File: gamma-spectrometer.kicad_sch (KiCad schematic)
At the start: 62 parts, among them J1 *, J2 *, J3 *, J4 *, Q1 2N7002, Q2 2N7002, SW1 *, U1 Pico 2, U2 OPA357AIDBVR, U3 TLV3201AIDBVR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

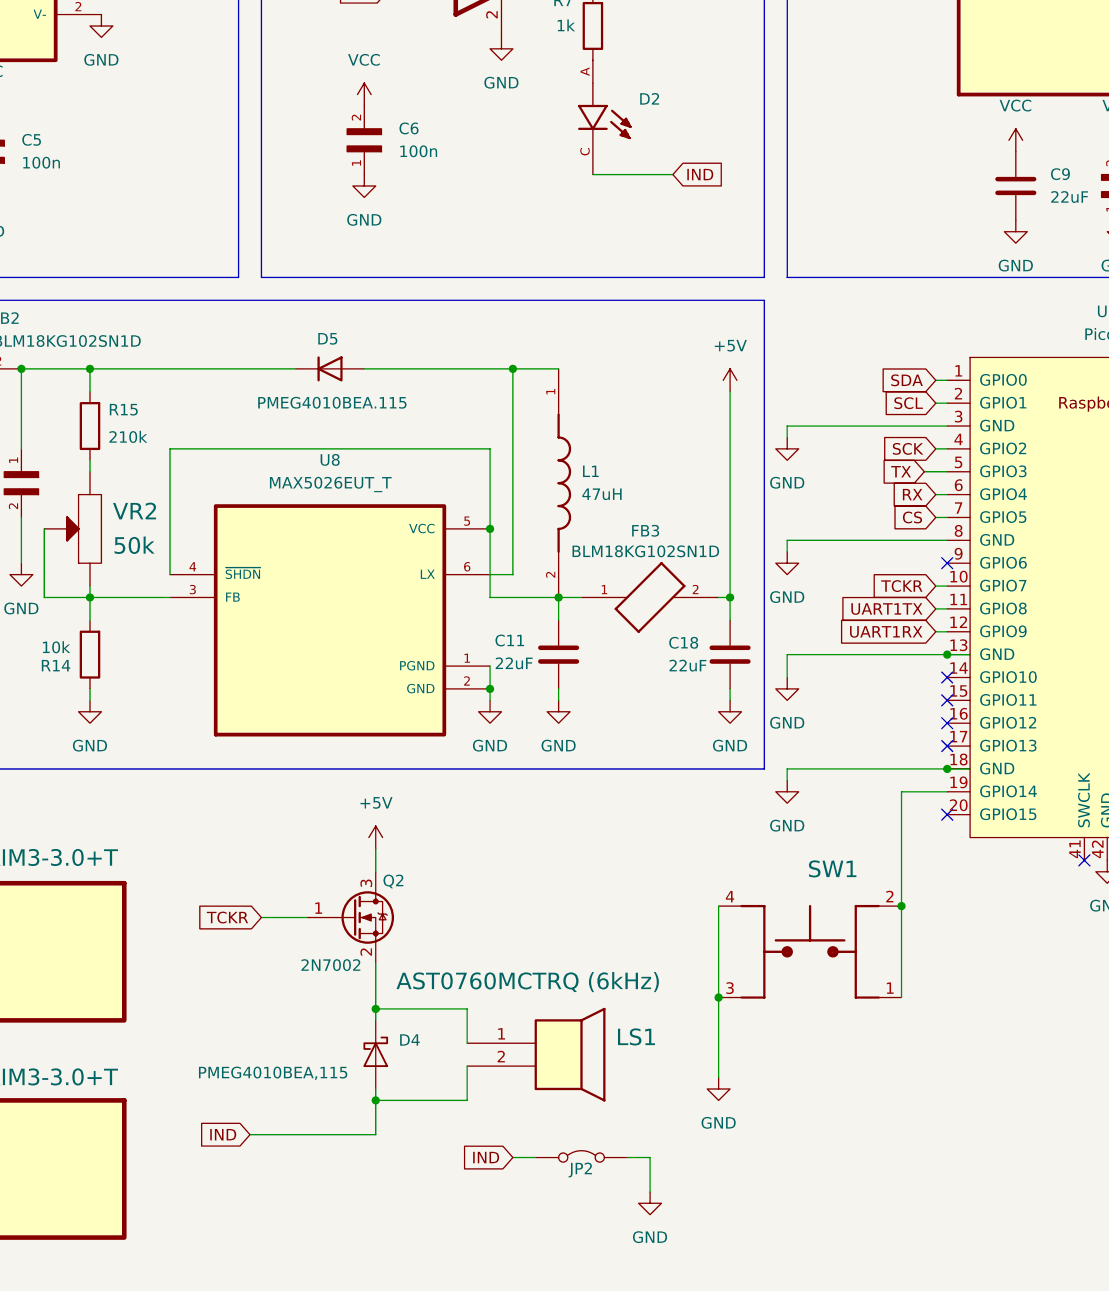
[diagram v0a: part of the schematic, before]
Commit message: Changed schematic for default I2C pins
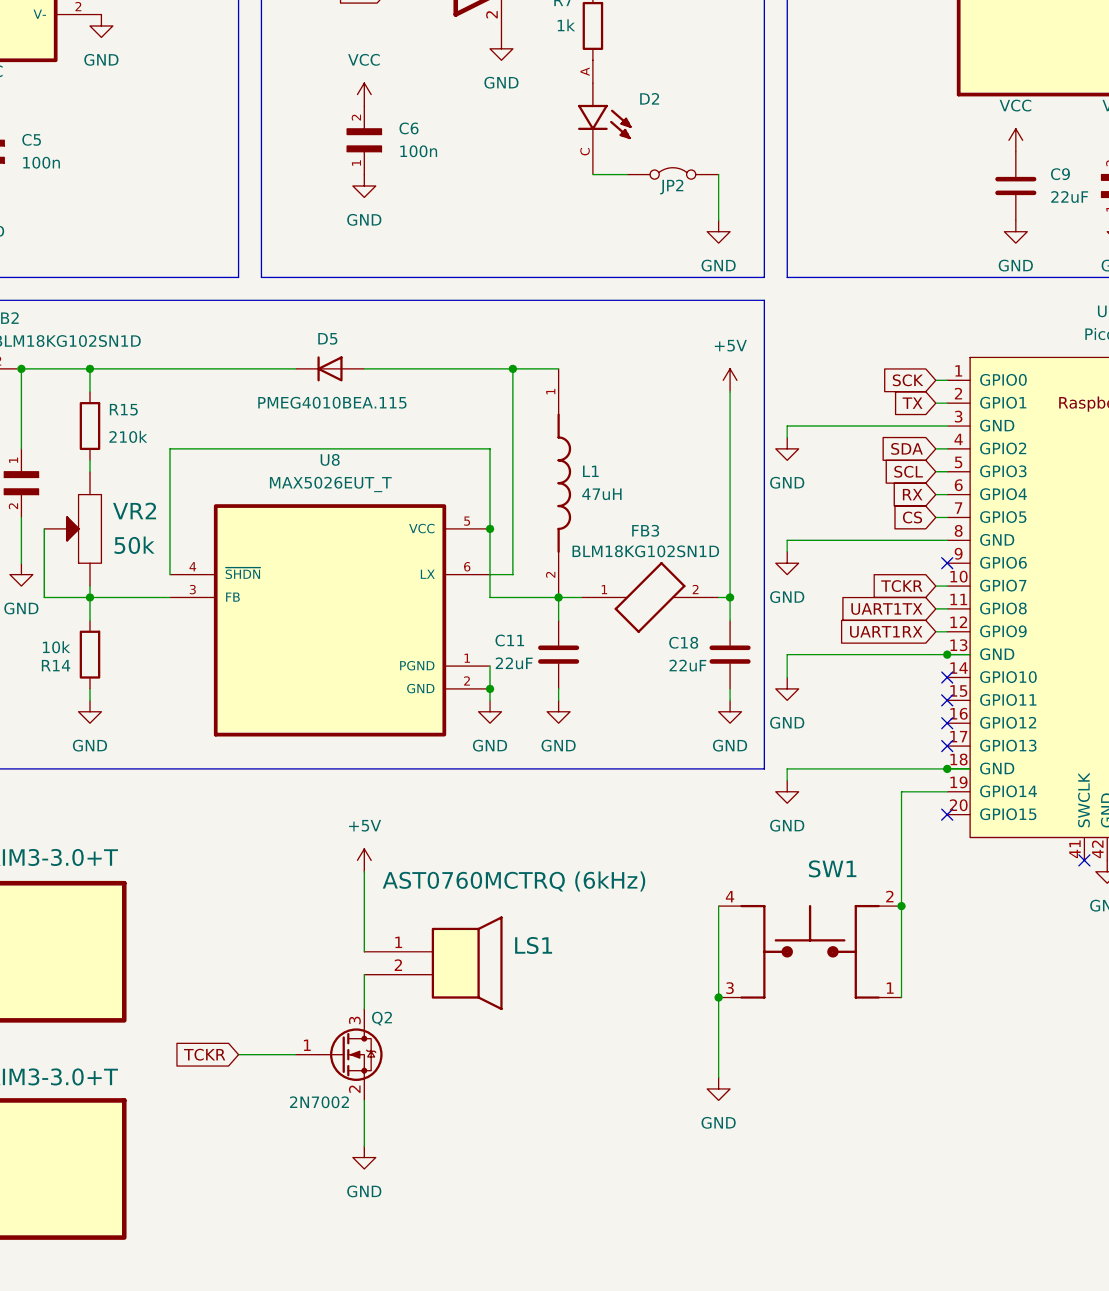
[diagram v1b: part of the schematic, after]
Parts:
- removed D4: PMEG4010BEA,115, Diode_SMD:D_SOD-323F, symbol Diode:PMEG4010EJ
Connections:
- net +5V: now also LS1.1; no longer Q2.3 (D)
- net GND: now also Q2.2 (S)
- net SCK: now also U1.1 (GPIO0); no longer U1.4 (GPIO2)
- net SCL: now also U1.5 (GPIO3); no longer U1.2 (GPIO1)
- net SDA: now also U1.4 (GPIO2); no longer U1.1 (GPIO0)
- net TX: now also U1.2 (GPIO1); no longer U1.5 (GPIO3)
- net IND: no longer names the net of D2.C, JP2.1 (A)
- net IND: no longer LS1.2
- new net: LS1.2, Q2.3 (D)
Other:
- moved on the sheet: JP2, LS1

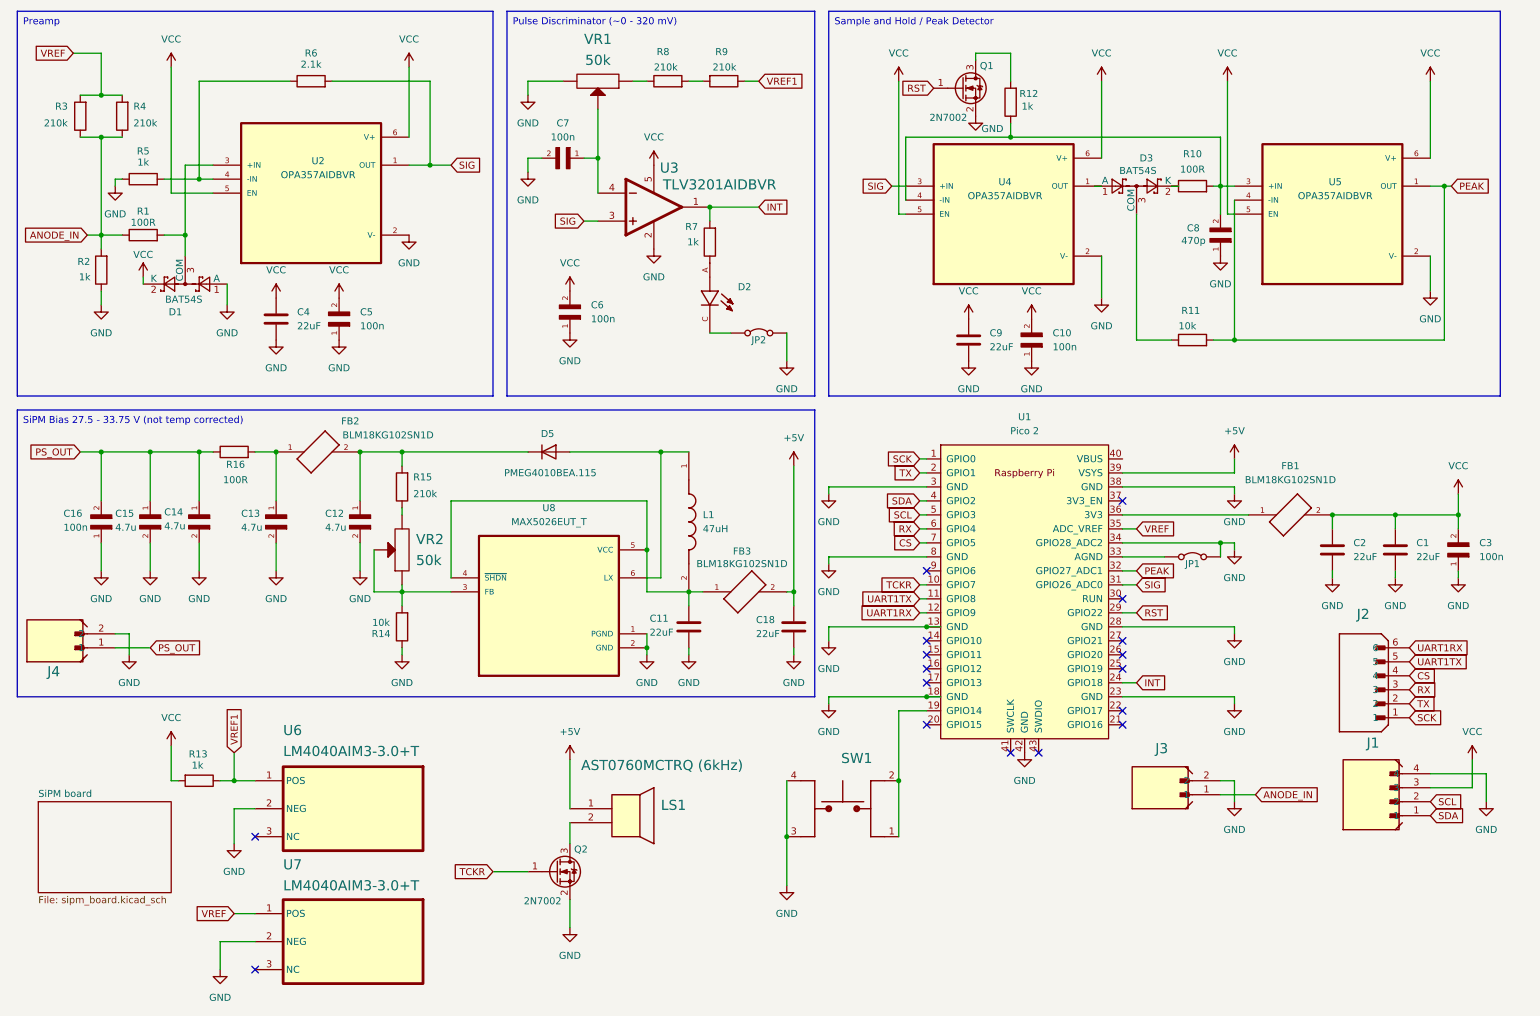
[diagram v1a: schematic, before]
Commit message: Added gain regulator. MHF3 connector for signal line.
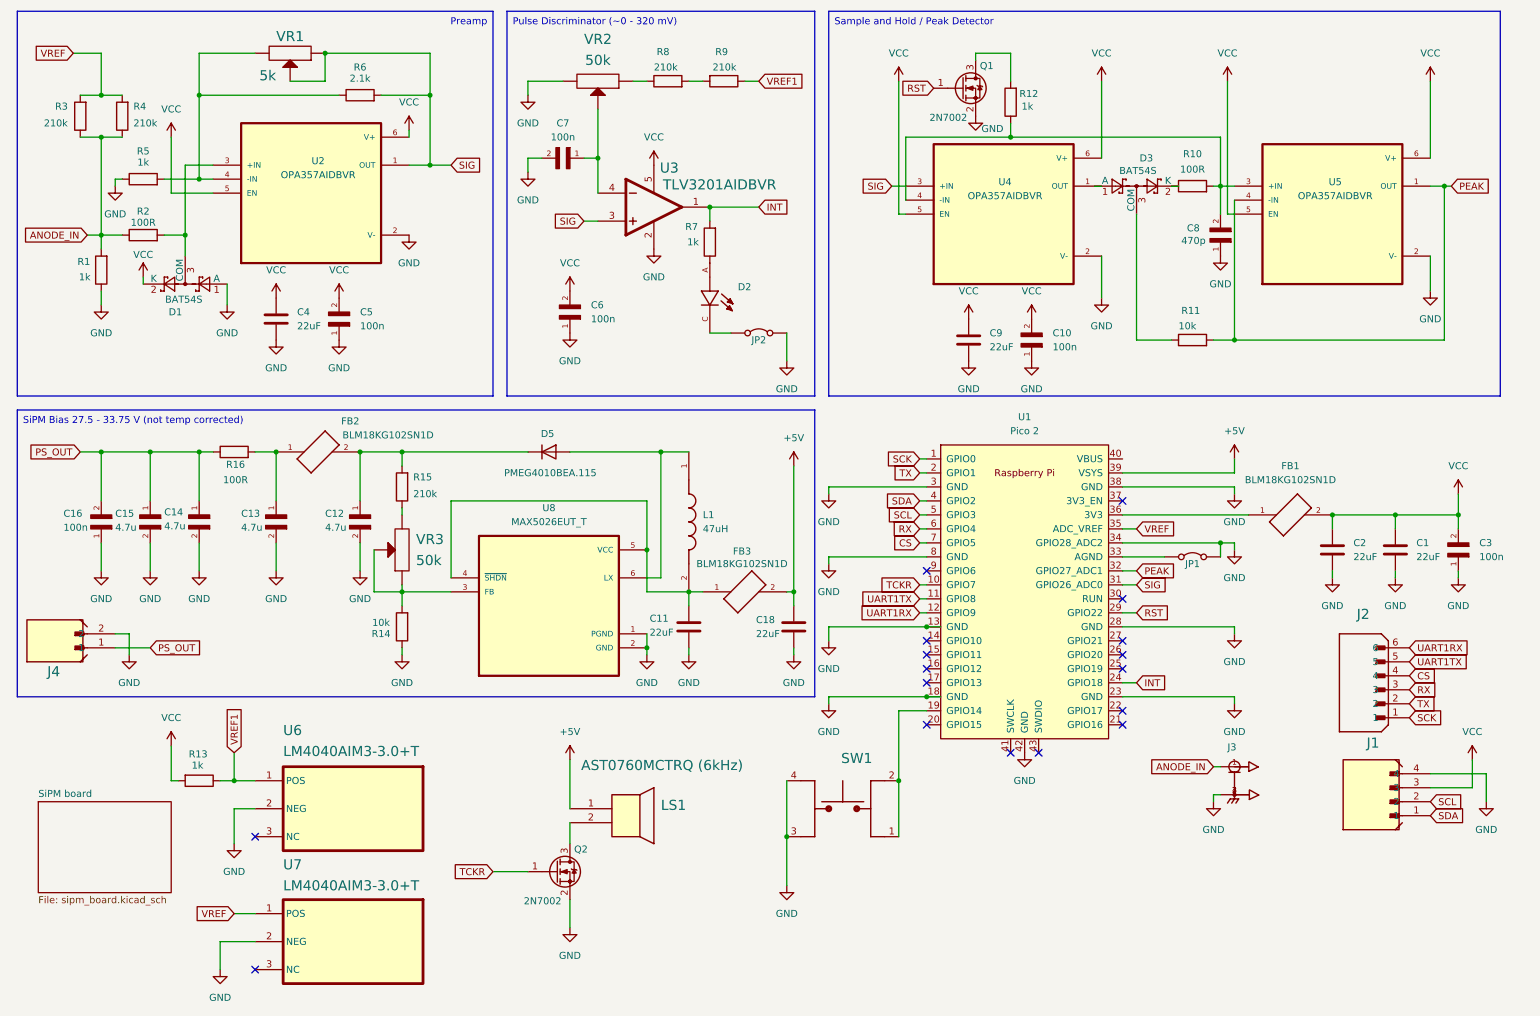
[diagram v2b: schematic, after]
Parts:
- removed J3: *, B2B-PH-K-S_LF__SN_:JST_B2B-PH-K-S(LF)(SN), symbol B2B-PH-K-S_LF__SN_:B2B-PH-K-S(LF)(SN)
- added J3: 20449-001E-03, 20449-001E-03:IPEX_20449-001E-03, symbol 20449-001E-03:20449-001E-03
- added VR1: 5k, 3296W-1-502LF:TRIM_3296W-1-502LF, symbol 3296W-1-502LF-1:3296W-1-502LF_1
- renumbered R2 to R1, R1 to R2, VR1 to VR2, VR2 to VR3
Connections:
- net ANODE_IN: now also J3.1
- net GND: now also J3.2, J3.3, J3.4
- net SIG: now also VR1.1 (CCW), VR1.2 (WIPER)
- net at R5.2, R6.1, U2.4 (-IN): now also VR1.3 (CW)
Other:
- moved on the sheet: R6

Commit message: BDG4-01 module boards design
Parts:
- removed C4: 22uF, CL10A226MP8NUNE:CAPC1608X90N, symbol Device:C
- removed C5: 100n, CL10B104KC8NNNC:CAPC1608X90N, symbol CL10B104KC8NNNC:CL10B104KC8NNNC
- removed D1: BAT54S, Package_TO_SOT_SMD:SOT-23, symbol Diode:BAT54S
- removed J3: 20449-001E-03, 20449-001E-03:IPEX_20449-001E-03, symbol 20449-001E-03:20449-001E-03
- removed J4: *, B2B-PH-K-S_LF__SN_:JST_B2B-PH-K-S(LF)(SN), symbol B2B-PH-K-S_LF__SN_:B2B-PH-K-S(LF)(SN)
- removed LS1: AST0760MCTRQ (6kHz), AST0760MCTRQ:AST0760_MAL, symbol AST0760MCTRQ:AST0760MCTRQ
- removed Q2: 2N7002, Package_TO_SOT_SMD:SOT-23, symbol Transistor_FET:2N7002
- removed R1, R5: 1k, ERJ3EKF2103V:RES_ERJ3EKF2103V, symbol Device:R
- removed R2: 100R, ERJ3EKF2103V:RES_ERJ3EKF2103V, symbol Device:R
- removed R3, R4: 210k, ERJ3EKF2103V:RES_ERJ3EKF2103V, symbol Device:R
- removed R6: 2.1k, ERJ3EKF2103V:RES_ERJ3EKF2103V, symbol Device:R
- removed SW1: *, SW_TL3305AF160QG:SW_TL3305AF160QG, symbol TL3305AF160QG:TL3305AF160QG
- removed U2: OPA357AIDBVR, OPA357AIDBVR:SOT95P280X145-6N, symbol OPA357AIDBVR:OPA357AIDBVR
- removed U7: LM4040AIM3-3.0+T, LM4040AIM3-3_0-T:SOT95P237X112-3N, symbol LM4040AIM3-3_0-T:LM4040AIM3-3_0-T
- removed VR1: 5k, 3296W-1-502LF:TRIM_3296W-1-502LF, symbol 3296W-1-502LF-1:3296W-1-502LF_1
- removed VR2: 50k, 3296W-1-503LF:TRIM_3296W-1-503LF, symbol 3296W-1-503LF:3296W-1-503LF
- added VR1: 50k, 3296W-1-503LF:TRIM_3296W-1-503LF, symbol 3296W-1-503LF:3296W-1-503LF
- R7: value 1k -> 210k
- R8: value 210k -> 1k
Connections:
- net GND: now also C6.2, C7.1, VR1.1 (CCW); no longer C6.1, C7.2
- net INT: now also R8.2; no longer R7.2
- net VCC: now also C7.2; no longer C6.2
- net VREF: now also R13.1, R9.1, U6.1 (POS); no longer U1.35 (ADC_VREF)
- net VREF1: now also U1.35 (ADC_VREF); no longer R13.1, R9.1, U6.1 (POS)
- net at C11.1, FB3.1, L1.2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: now also D5.2 (A), L1.1, U8.6 (LX)
- net at R7.1: now also VR1.3 (CW); no longer D2.A
- net at R9.2: now also R7.2; no longer R8.2
- net at R8.1: now also D2.A
- net at U3.4 (IN-): now also C6.1, VR1.2 (WIPER); no longer C7.1
- net VBUS: now reaches U1.40 (VBUS)
- net TCKR: no longer names the net of U1.10 (GPIO7)
- no-connect marks 17 -> 18
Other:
- added sheet Amplifier (preamp.kicad_sch)
- moved on the sheet: C1, C11, C12, C13, C14, C15, C16, C18, C2, C3, D5, FB1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

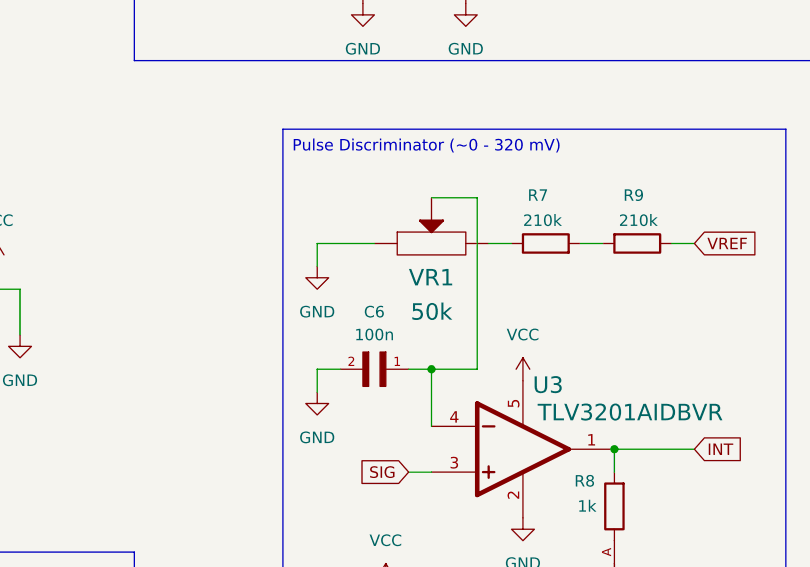
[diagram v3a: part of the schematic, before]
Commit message: PCB changes for more precise assembling
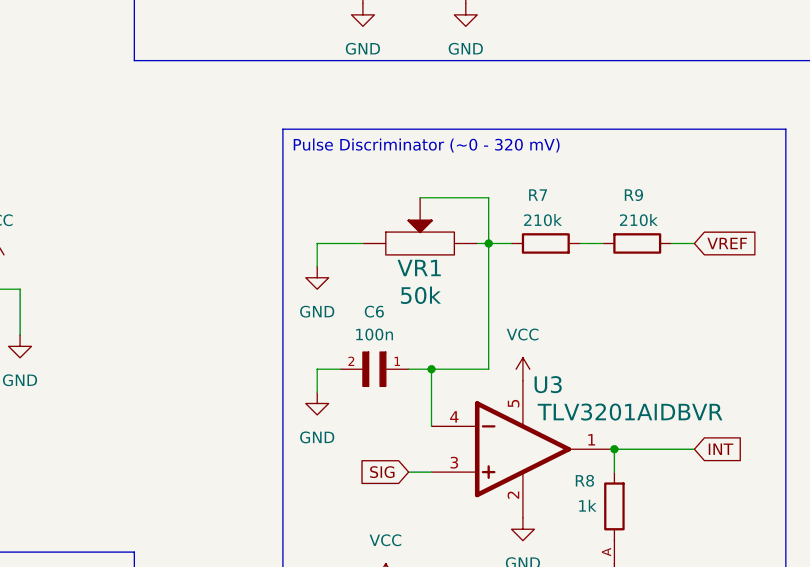
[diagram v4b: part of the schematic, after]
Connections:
- net at C6.1, U3.4 (IN-), VR1.2 (WIPER): now also R7.1, VR1.3 (CW)
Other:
- moved on the sheet: VR1
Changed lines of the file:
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@@
 		(title "Gamma Spectrometer")
 		(date "2025-01-17")
-		(rev "0.1.0")
+		(rev "0.1.1")
 		(company "Vadym Vikulin")
 	)
@@
 	)
 	(junction
+		(at 200.66 105.41)
+		(diameter 0)
+		(color 0 0 0 0)
+	)
+	(junction
 		(at 130.81 165.1)
 		(diameter 0)
@@
 	(wire
 		(pts
-			(xy 199.39 100.33) (xy 199.39 119.38)
+			(xy 200.66 105.41) (xy 200.66 119.38)
+		)
+		(stroke
+			(width 0)
+			(type default)
+		)
+	)
+	(wire
+		(pts
+			(xy 200.66 100.33) (xy 200.66 105.41)
 		)
 		(stroke
@@
 	(wire
 		(pts
-			(xy 181.61 105.41) (xy 187.96 105.41)
+			(xy 181.61 105.41) (xy 186.69 105.41)
 		)
 		(stroke
@@
 	(wire
 		(pts
-			(xy 199.39 119.38) (xy 194.31 119.38)
+			(xy 200.66 119.38) (xy 194.31 119.38)
 		)
 		(stroke
@@
 	(wire
 		(pts
-			(xy 199.39 100.33) (xy 194.31 100.33)
+			(xy 200.66 100.33) (xy 193.04 100.33)
 		)
 		(stroke
@@
 	(wire
 		(pts
+			(xy 199.39 105.41) (xy 200.66 105.41)
+		)
+		(stroke
+			(width 0)
+			(type default)
+		)
+	)
+	(wire
+		(pts
 			(xy 157.48 172.72) (xy 156.21 172.72)
 		)
@@
 	(wire
 		(pts
-			(xy 45.72 67.31) (xy 27.94 67.31)
+			(xy 200.66 105.41) (xy 203.2 105.41)
 		)
 		(stroke
@@
 	(wire
 		(pts
-			(xy 101.6 68.58) (xy 101.6 67.31)
+			(xy 45.72 67.31) (xy 27.94 67.31)
 		)
 		(stroke
@@
 	(wire
 		(pts
-			(xy 39.37 105.41) (xy 45.72 105.41)
+			(xy 101.6 68.58) (xy 101.6 67.31)
 		)
 		(stroke
@@
 	(wire
 		(pts
-			(xy 194.31 27.94) (xy 194.31 22.86)
+			(xy 39.37 105.41) (xy 45.72 105.41)
 		)
 		(stroke
@@
 	(wire
 		(pts
-			(xy 86.36 158.75) (xy 86.36 157.48)
+			(xy 194.31 27.94) (xy 194.31 22.86)
 		)
 		(stroke
@@
 	(wire
 		(pts
-			(xy 200.66 105.41) (xy 203.2 105.41)
+			(xy 86.36 158.75) (xy 86.36 157.48)
 		)
 		(stroke
@@
 		(lib_name "3296W-1-503LF_1")
 		(lib_id "3296W-1-503LF:3296W-1-503LF")
-		(at 194.31 105.41 0)
+		(at 193.04 105.41 0)
 		(unit 1)
 		(exclude_from_sim no)
@@
 		(on_board yes)
 		(dnp no)
-		(fields_autoplaced yes)
 		(property "Reference" "VR1"
-			(at 194.31 109.22 0)
+			(at 193.04 108.204 0)
 			(effects
 				(font
@@
 		)
 		(property "Value" "50k"
-			(at 194.31 113.03 0)
+			(at 193.04 111.252 0)
 			(effects
 				(font
@@
 		)
 		(property "Footprint" "3296W-1-503LF:TRIM_3296W-1-503LF"
-			(at 194.31 91.44 0)
+			(at 193.04 91.44 0)
 			(effects
 				(font
@@
 		)
 		(property "Datasheet" ""
-			(at 194.31 105.41 0)
+			(at 193.04 105.41 0)
 			(effects
 				(font
@@
 		)
 		(property "Description" "50 kOhms 0.5W, 1/2W PC Pins Through Hole Trimmer Potentiometer Cermet 25.0 Turn Top Adjustment"
-			(at 195.072 111.252 0)
+			(at 193.802 111.252 0)
 			(effects
 				(font
@@
 		)
 		(property "MF" "Bourns"
-			(at 189.738 113.538 0)
+			(at 188.468 113.538 0)
 			(effects
 				(font
@@
 		)
 		(property "Purchase-URL" "https://pricing.snapeda.com/search/part/3296W-1-503LF/?ref=eda"
-			(at 174.244 116.078 0)
+			(at 172.974 116.078 0)
 			(effects
 				(font
@@
 		)
 		(property "ALTIUM_VALUE" "*"
-			(at 196.596 102.362 0)
+			(at 195.326 102.362 0)
 			(effects
 				(font
@@
 		)
 		(property "SnapEDA_Link" "https://www.snapeda.com/parts/3296W-1-503LF/Bourns/view-part/?ref=snap"
-			(at 173.228 121.158 0)
+			(at 171.958 121.158 0)
 			(effects
 				(font
@@
 		)
 		(property "Package" "SOT-23-5 Bourns"
-			(at 182.118 140.716 0)
+			(at 180.848 140.716 0)
 			(effects
 				(font
@@
 		)
 		(property "Availability" "In Stock"
-			(at 188.976 136.144 0)
+			(at 187.706 136.144 0)
 			(effects
 				(font
@@
 		)
 		(property "Price" "None"
-			(at 191.008 118.618 0)
+			(at 189.738 118.618 0)
 			(effects
 				(font
@@
 		)
 		(property "Check_prices" "https://www.snapeda.com/parts/3296W-1-503LF/Bourns/view-part/?ref=eda"
-			(at 173.482 129.794 0)
+			(at 172.212 129.794 0)
 			(effects
 				(font
@@
 		)
 		(property "MP" "3296W-1-503LF"
-			(at 180.34 124.968 0)
+			(at 179.07 124.968 0)
 			(effects
 				(font
